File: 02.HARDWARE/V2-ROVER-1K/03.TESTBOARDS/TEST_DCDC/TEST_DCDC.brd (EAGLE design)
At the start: 98 x 70 mm, 47 parts, among them J1 FEMALE 2x3, J2 OSTVN03A150, J3 OSTVN03A150, J4 OSTVN03A150, Q1 PJA3416AE_R1_00001, Q2 PJA3416AE_R1_00001, Q3 PJA3416AE_R1_00001, U3 ATE1D-5M3-10-Z, U6 AP62200WU-7

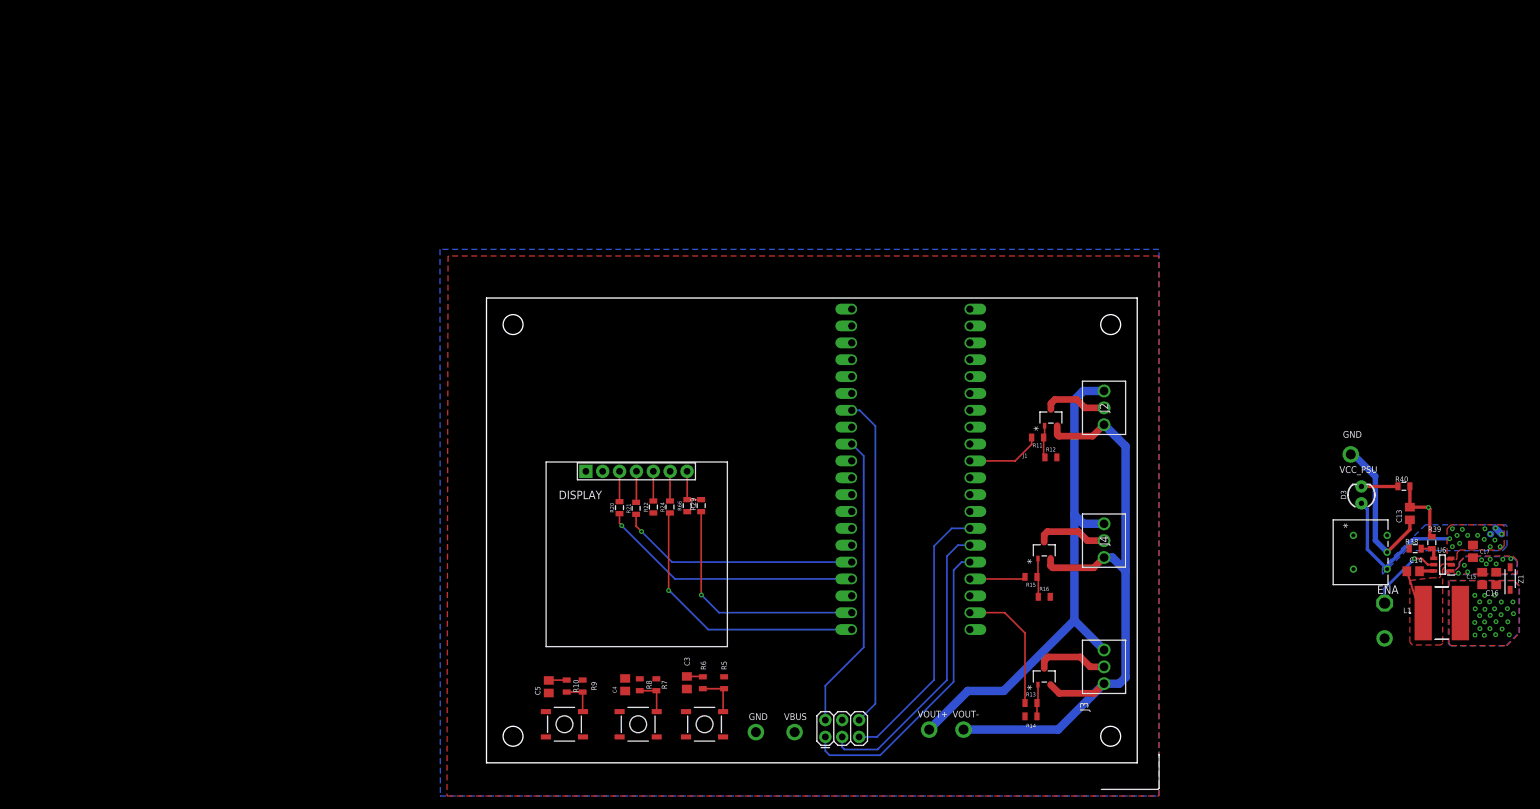
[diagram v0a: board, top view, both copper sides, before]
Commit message: wip previo a envio PCBWAY
Queda revisar todavia y rutear
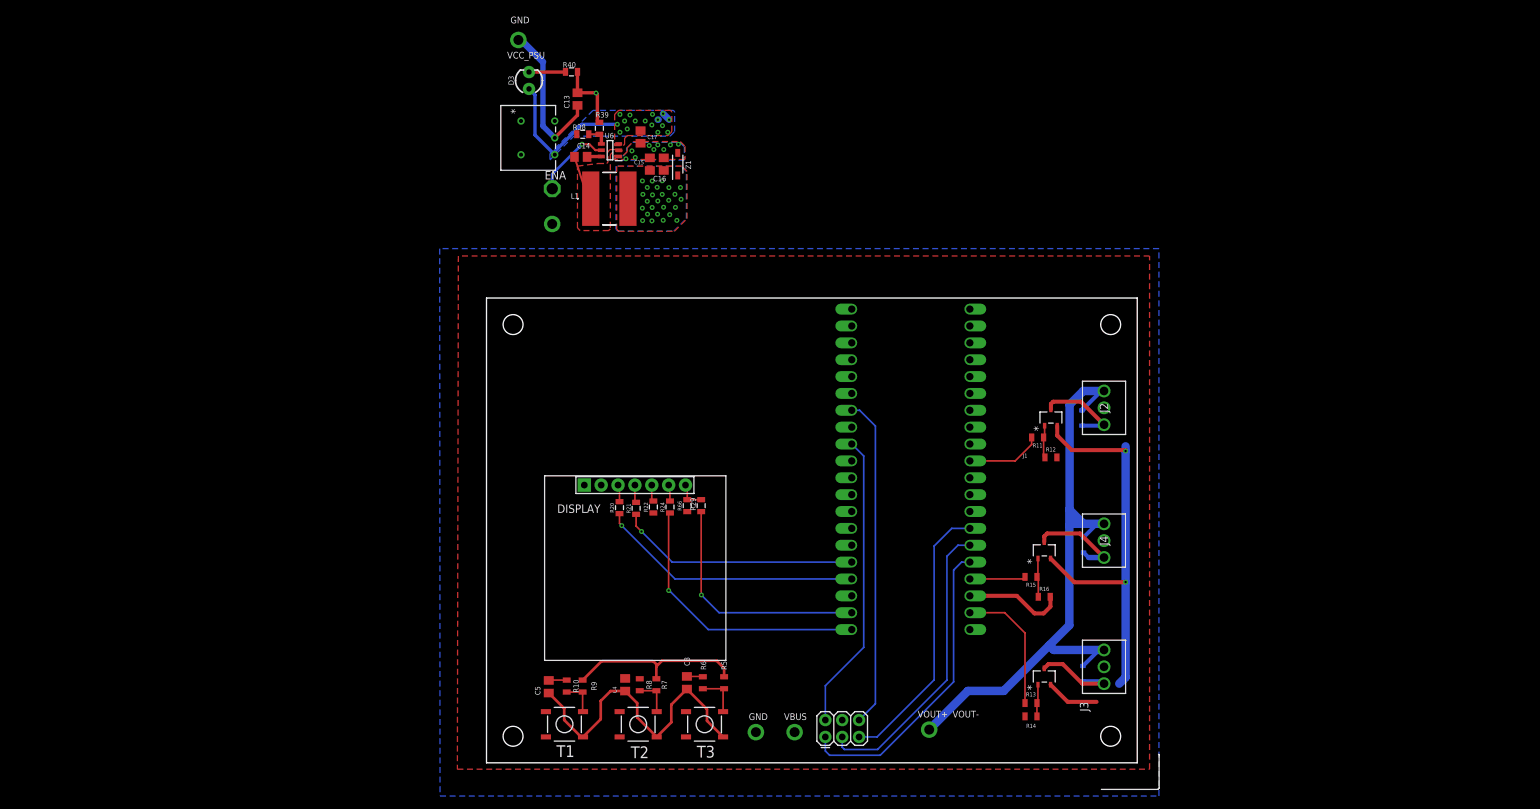
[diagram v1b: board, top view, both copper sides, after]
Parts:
- added D1, D2, D4: 250mA/100V, SparkFun-DiscreteSemi:SOD-323
- moved C13 140.0 mm to (13.7, 100.0)
- moved C14 140.0 mm to (14.2, 91.3)
- moved C15 140.0 mm to (24.6, 90.2)
- moved C16 140.0 mm to (26.7, 90.2)
- moved C17 140.0 mm to (23.2, 94.3)
- moved L1 140.0 mm to (18.5, 85.0)
- moved R38 140.0 mm to (14.5, 94.7)
- moved R39 140.0 mm to (17.0, 95.6)
- moved R40 140.0 mm to (12.8, 104.1)
- moved U3 140.0 mm to (5.20, 96.7)
- moved U6 140.0 mm to (18.6, 92.3)
- moved Z1 140.0 mm to (28.8, 90.2)
- moved D3 140.0 mm to (6.40, 102.8)
- moved ENA 140.0 mm to (9.90, 86.5)
- moved DISPLAY 2.08 mm to (22.1, 28.1)
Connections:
- removed net N$18: J3.2, Q2.3
- removed net N$26: J4.2, Q3.3
- removed net N$8: J2.2, Q1.3
- new net N$1: D4.A, J4.3, Q3.3
- new net N$21: D1.A, J2.3, Q1.3
- new net N$3: D2.A, J3.3, Q2.3
- net VOUT+: now also D1.C, D2.C, D4.C
- net VOUT-: no longer J2.3, J3.3, J4.3
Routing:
- net GND: track 10.6 -> 72.9 mm
- net VOUT-: track 99.4 -> 69.8 mm, vias 1 -> 2
- net VCC: track 0.00 -> 27.0 mm
- net VOUT+: track 78.3 -> 96.5 mm
- net N$1: track 0.00 -> 14.9 mm
- net N$3: track 0.00 -> 13.8 mm
- net N$21: track 0.00 -> 13.8 mm
- net N$18: track 11.0 -> 0.00 mm
- net N$26: track 10.9 -> 0.00 mm
- net N$8: track 9.66 -> 0.00 mm
- net D1: track 4.69 -> 2.67 mm
- net N$17: track 4.48 -> 2.48 mm
- net D0: track 4.57 -> 2.59 mm
- net RST: track 4.47 -> 2.50 mm
- net CS: track 6.38 -> 4.41 mm
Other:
- board text added: "T1"
- board text added: "T2"
- board text added: "T3"

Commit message: Version 1 pendiente de revision
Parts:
- removed C14, C15, C16, C17: (no value), rcl:C0805
- removed ENA: TESTPAD_TPSQPAD1-17, BeagleBone_Blue_R3:TESTPAD_P1-17
- removed L1: SRN8040-8R2Y, SRN8040-8R2Y:SRN80408R2Y
- removed R38, R39: 10K, SparkFun:0805
- removed U6: AP62200WU-7, AP62200WU-7:SOT95P280X100-6N
- added C1, C2: 100n, rcl:C0805
- added D5: (no value), SparkFun-LED:LED_3MM
- added J5: ACJS-MHDR, ACJSMHDR:CONN_MHDR_AMP
- added J6, J7, J8, J9: (no value), SparkFun-Connectors:1X02
- added JP1: JUMPER-SMT_3_1-NC_PASTE_SILK, SparkFun-Jumpers:SMT-JUMPER_3_1-NC_PASTE_SILK
- added Q4: 310mA/60V/1.6Ω, SparkFun-DiscreteSemi:SOT323
- added R1: (no value), SparkFun-Resistors:0805
- added R2, R3: 10K, SparkFun-Resistors:0805
- added R4: 10K, SparkFun:0805
- added U1: MCP4725, SparkFun-IC-Conversion:SOT23-6
- moved J3 97.0 mm to (6.00, 60.0)
- moved J4 94.9 mm to (6.00, 74.0)
- moved J2 92.4 mm to (6.00, 87.0)
- moved D2 91.4 mm to (9.80, 57.5)
- moved D4 89.1 mm to (9.67, 71.4)
- moved D1 86.3 mm to (9.64, 84.3)
- moved Z1 80.4 mm to (12.6, 11.4), turned to 0 degrees
- moved Q2 80.3 mm to (15.5, 54.9), turned to 180 degrees
- moved C13 79.0 mm to (10.3, 21.0), turned to 90 degrees
- moved Q3 77.9 mm to (15.5, 69.0), turned to 180 degrees
- moved R14 76.7 mm to (24.0, 57.1), turned to 90 degrees
- moved Q1 75.7 mm to (15.5, 82.0), turned to 180 degrees
- moved R16 74.6 mm to (25.2, 70.9), turned to 90 degrees
- moved R13 72.7 mm to (24.9, 54.0), turned to 0 degrees
- moved R12 71.7 mm to (24.3, 84.2), turned to 90 degrees
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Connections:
- removed net EN_LDO: ENA.TP, U6.5
- removed net N$23: U4.GP9
- removed net N$31: C14.2, U6.6
- removed net N$32: C14.1, L1.1, U6.2
- removed net N$33: R38.1, R39.2, U6.4
- removed net TEST_4: U4.GP20
- removed net TEST_5: U4.GP15
- removed net VBUSBAR: C17.1, D3.A, U3.1, U6.3
- removed net VCC_PSU: C13.2, U3.2
- new net FB_DAC_PWM: JP1.3, U4.GP11
- new net N$18: JP1.1, U1.1
- new net N$26: D5.K, R4.2
- new net N$27: D5.A, U4.VBUS
- new net OP_SWITCH_CPU: Q4.1, U4.GP10
- new net VBUS: D3.A, U3.1, Z1.1
- new net VBUS_PSU: C13.2, J6.1, J6.2, U3.2
- net DSP_RST: now also U4.GP12
- net EN_DCDC: now also U4.GP9; no longer U4.GP11
- net FB_DAC: now also JP1.2; no longer U4.GP12
- net GND: now also C1.1, C2.1, J7.1, J7.2, Q4.2, R4.1, U1.2, U1.6; no longer C15.1, C16.1, C17.2, R39.1, U6.1
- net IOSENSE: now also U4.GP28_A2; no longer U4.GP27_A1
- net OP_SWITCH: now also Q4.3, R1.1; no longer U4.GP10
- net R1: now also U4.GP22; no longer U4.GP7
- net R2: now also U4.GP21; no longer U4.GP13
- net R3: now also U4.GP20; no longer U4.GP14
- net SCL: now also R2.1, U1.5
- net SDA: now also R3.1, U1.4
- net TEST_1: now also U4.GP15; no longer U4.GP26_A0
- net TEST_2: now also U4.GP14; no longer U4.GP22
- net TEST_3: now also U4.GP13; no longer U4.GP21
- net VCC: now also C1.2, C2.2, R1.2, R2.2, R3.2, U1.3, U4.3V3; no longer C15.2, C16.2, L1.2, R38.2, U4.VBUS, Z1.1
- net VOUT+: now also J5.6, J8.1, J8.2
- net VOUT-: now also J5.1, J5.4, J5.5, J9.1, J9.2
- net VOUTSENSE: now also U4.GP27_A1; no longer U4.GP28_A2
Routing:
- net VOUT-: track 69.8 -> 229.5 mm, vias 2 -> 1
- net FB_DAC: track 46.0 -> 145.0 mm, vias 0 -> 1
- net EN_DCDC: track 44.6 -> 111.0 mm, vias 0 -> 1
- net GND: track 72.9 -> 136.3 mm, vias 12 -> 9
- net TEST_3: track 2.42 -> 60.1 mm
- net OP_SWITCH: track 41.5 -> 96.5 mm
- net TEST_2: track 0.00 -> 54.3 mm
- net TEST_1: track 2.72 -> 55.0 mm
- net IOSENSE: track 44.7 -> 93.2 mm, vias 0 -> 1
- net VBUS: track 0.00 -> 43.4 mm
- net VOUT+: track 96.5 -> 136.3 mm
- net VOUTSENSE: track 49.8 -> 87.7 mm, vias 0 -> 1
- net VBUS_PSU: track 0.00 -> 27.1 mm, vias 0 -> 1
- net R1: track 11.4 -> 38.3 mm, vias 0 -> 2
- net MISO: track 41.8 -> 15.4 mm
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- added copper zone on layer 16, net VBUS
- added copper zone on layer 16, net VOUT+
- added copper zone on layer 16, net VOUT-
- removed copper zone on layer 1, net N$32
- removed copper zone on layer 1, net VBUSBAR
- removed copper zone on layer 16, net VBUSBAR
- removed copper zone on layer 16, net VCC
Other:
- board size 98 x 70 mm -> 93 x 100 mm
- board text added: "TEST_DCDC Rover R1 Ene'23- v1"
- board text added: "VBUS_PSU"
- board text removed: "Carrier Motor Driver v1-Sep22"
- board text removed: "MUSOTOKU"
- board text removed: "T1"
- board text removed: "T2"
- board text removed: "T3"
- board text removed: "VCC_PSU"

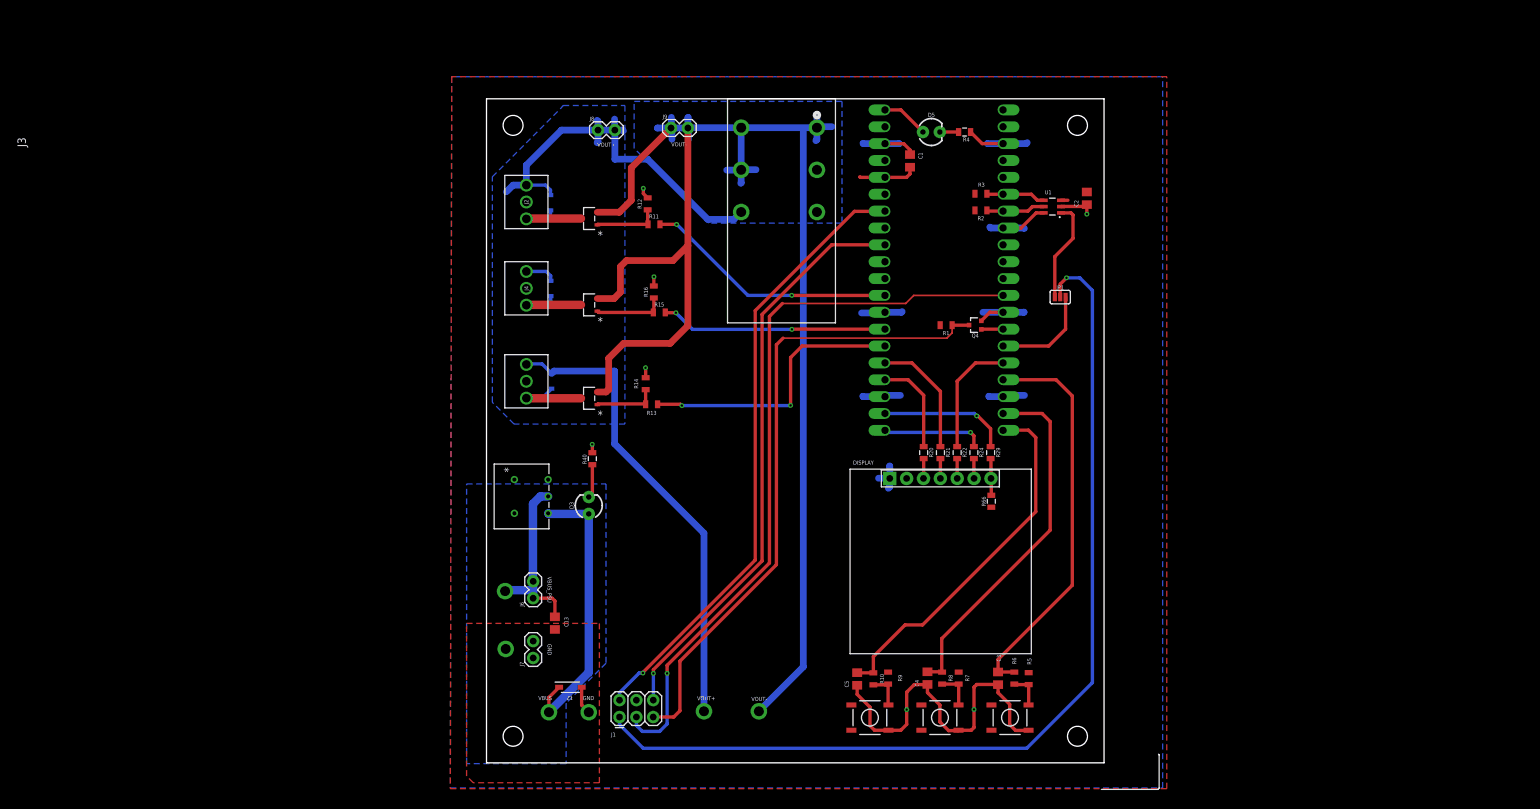
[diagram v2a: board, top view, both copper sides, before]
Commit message: Pedido PCBWAY ene-23 - revision despues de diseño
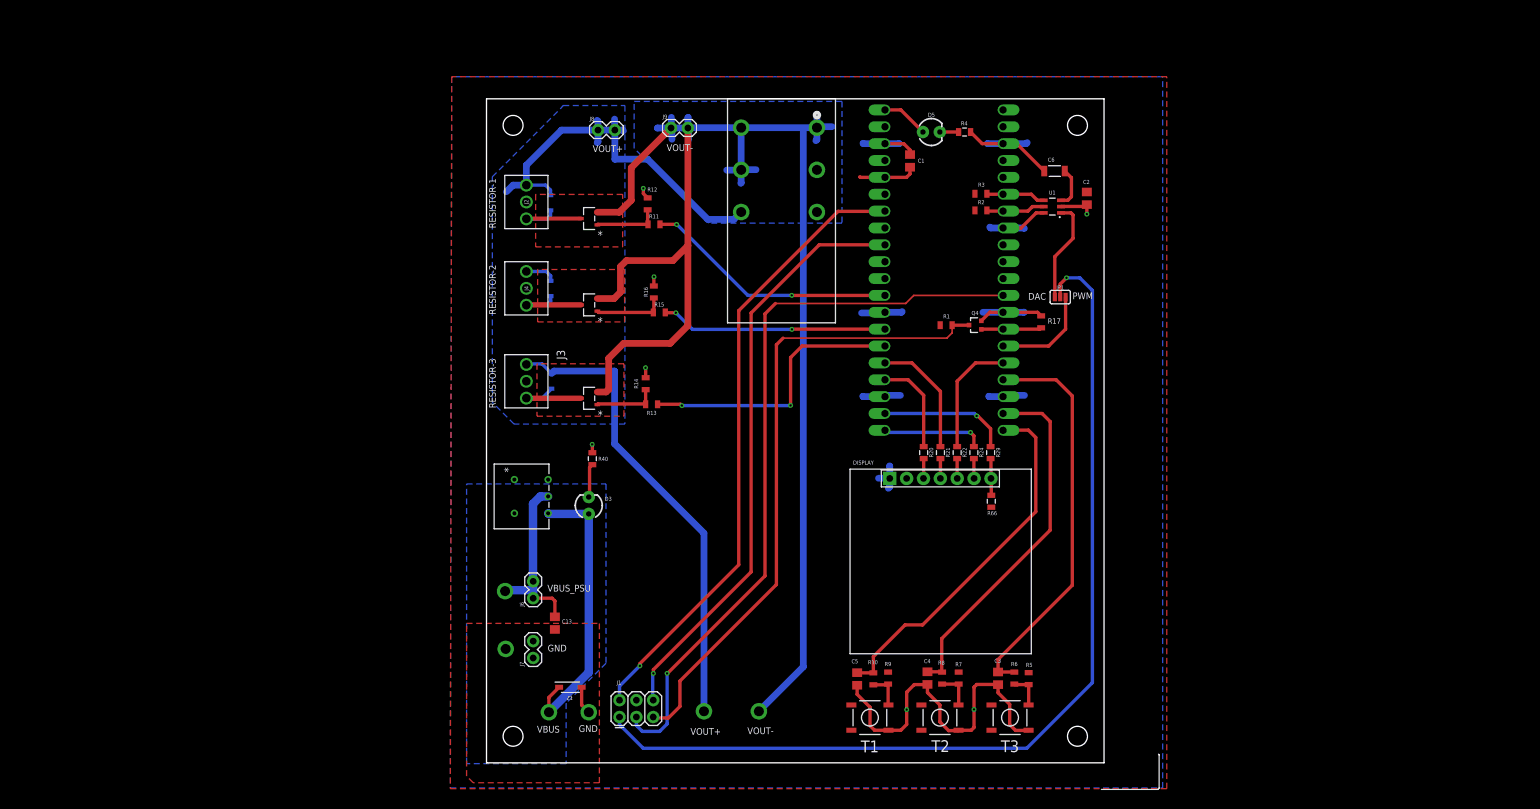
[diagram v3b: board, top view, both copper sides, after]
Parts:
- added C6: 10uF, Wurth_Elektronik_Passive_Capacitors_rev19a:WCAP-CSGP_1206
- added R17: 33k, SparkFun-Resistors:0805
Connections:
- net N$1 renamed R2_OUT
- net N$21 renamed R1_OUT
- net N$3 renamed R3_OUT
- net GND: now also C6.1, R17.1
- net OP_SWITCH_CPU: now also R17.2
- net VCC: now also C6.2
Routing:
- net GND: track 136.3 -> 150.1 mm
- net OP_SWITCH_CPU: track 3.28 -> 9.10 mm
- net VCC: track 9.86 -> 14.9 mm
- net VOUTSENSE: track 87.7 -> 88.9 mm
- net IOSENSE: track 93.2 -> 94.3 mm
- net EN_DCDC: track 111.0 -> 111.6 mm
- added copper zone on layer 1, net R1_OUT
- added copper zone on layer 1, net R2_OUT
- added copper zone on layer 1, net R3_OUT
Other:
- board text added: "DAC"
- board text added: "PWM"
- board text added: "RESISTOR-1"
- board text added: "RESISTOR-2"
- board text added: "RESISTOR-3"
- board text added: "T1"
- board text added: "T2"
- board text added: "T3"
